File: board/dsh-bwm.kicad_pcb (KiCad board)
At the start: 2 copper layers, 121.3 x 78.7 mm, 36 parts, among them IC1 TPS5450DDA, IC2 MAX485CSA+T, J1 MPM-15-24, J2 Power, J3 Connections, J4 LED, J5 SWD6p, K1 833H-1C-C-24VDC, K2 833H-1C-C-24VDC, K3 833H-1C-C-24VDC, K4 833H-1C-C-24VDC, Q1 IRLB8721PBF, SW1 BOOTSEL, U1 RP2040_Stamp

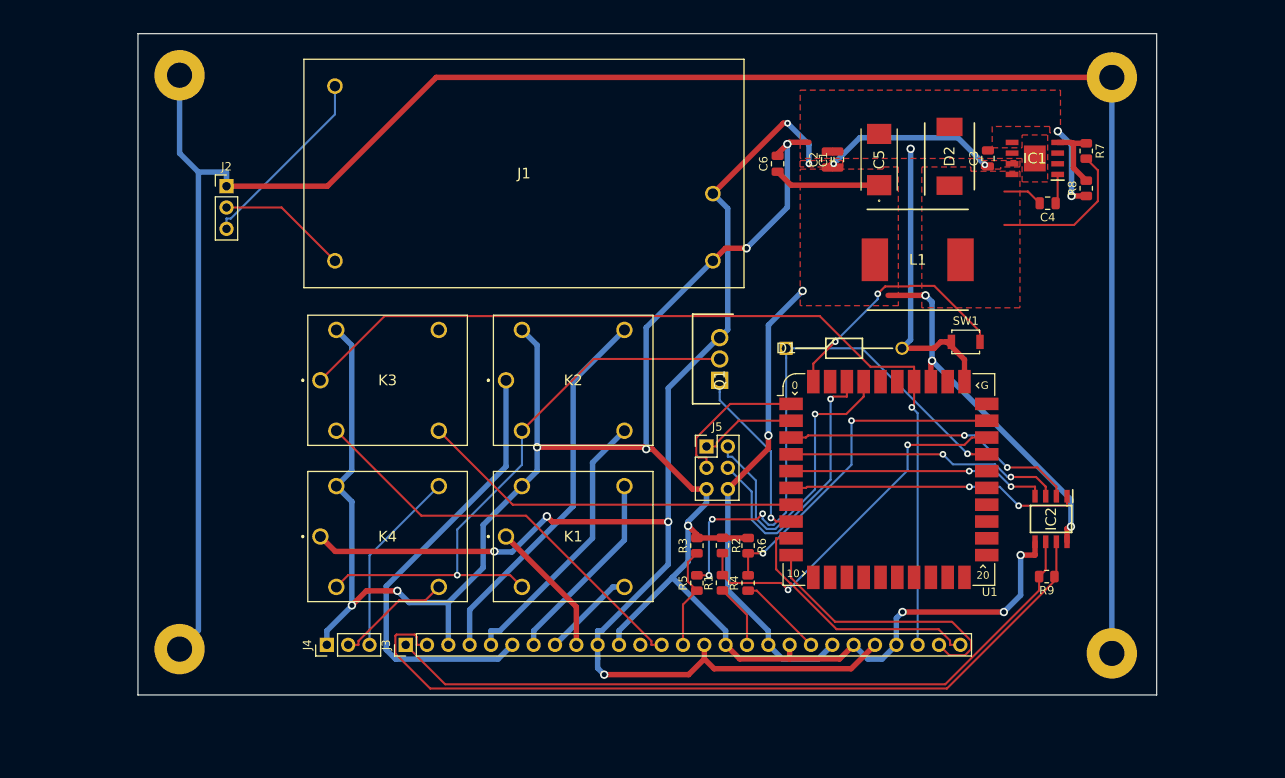
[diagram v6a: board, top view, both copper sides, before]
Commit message: board update, modbus address selector
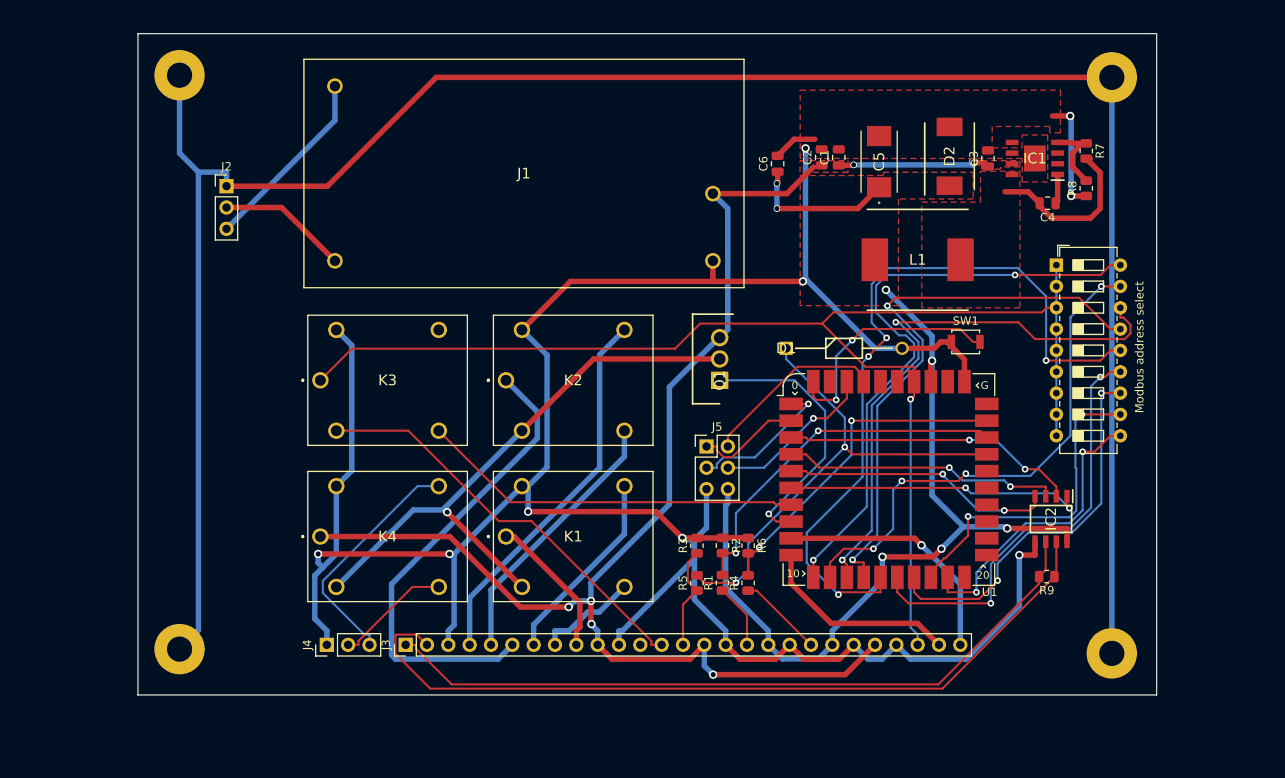
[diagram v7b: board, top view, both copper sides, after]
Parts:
- added Modbus address select: SW_DIP_x09, Button_Switch_THT:SW_DIP_SPSTx09_Slide_6.7x24.42mm_W7.62mm_P2.54mm_LowProfile, F.Cu at (200.9, 82.8)
- moved C2 0.77 mm to (173.0, 70.0)
- moved C1 0.30 mm to (175.0, 70.0)
- moved C5 0.25 mm to (179.8, 70.5)
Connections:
- D2 pad 1: /Power/5Vunf -> 5V
- U1 pad 11: unconnected-(U1-Pad11) -> MBADRB1
- U1 pad 12: unconnected-(U1-Pad12) -> MBADRB2
- U1 pad 13: unconnected-(U1-Pad13) -> MBADRB3
- U1 pad 14: unconnected-(U1-Pad14) -> MBADRB4
- U1 pad 15: unconnected-(U1-Pad15) -> MBADRB5
- U1 pad 16: unconnected-(U1-Pad16) -> MBADRB7
- U1 pad 17: unconnected-(U1-Pad17) -> MBADRB6
- U1 pad 18: unconnected-(U1-Pad18) -> MBADRB8
- U1 pad 19: unconnected-(U1-Pad19) -> MBADRB9
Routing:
- net MBADRB5: track 0.00 -> 90.0 mm, vias 0 -> 4
- net MBADRB1: track 0.00 -> 72.2 mm, vias 0 -> 2
- net MBADRB3: track 0.00 -> 68.5 mm, vias 0 -> 2
- net MBADRB4: track 0.00 -> 68.4 mm, vias 0 -> 2
- net MBADRB2: track 0.00 -> 61.2 mm, vias 0 -> 4
- net MBADRB7: track 0.00 -> 51.5 mm, vias 0 -> 2
- net 3v3: track 109.9 -> 158.3 mm
- net MBADRB6: track 0.00 -> 45.7 mm, vias 0 -> 2
- net MBADRB8: track 0.00 -> 38.8 mm, vias 0 -> 2
- net MBADRB9: track 0.00 -> 35.5 mm, vias 0 -> 2
- net 24V: track 186.0 -> 167.8 mm, vias 8 -> 6
- net SWDIO: track 37.1 -> 22.0 mm, vias 1 -> 0
- net GND: track 307.5 -> 321.5 mm, vias 13 -> 9
- net SWCLK: track 33.5 -> 19.6 mm
- net ALARM: track 21.5 -> 32.2 mm
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
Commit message: TPs, vias, some comments on board, fml
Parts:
- removed the J3 at (123.4, 128.0)
- removed Modbus address select: SW_DIP_x09, Button_Switch_THT:SW_DIP_SPSTx09_Slide_6.7x24.42mm_W7.62mm_P2.54mm_LowProfile
- removed the R1 at (161.2, 120.6)
- removed the R2 at (161.2, 116.2)
- added IC2: AT24C256C-SSHL-T, SamacSys_Parts:SOIC127P600X175-8N, F.Cu at (207.8, 115.6)
- added J1: USB_A, Connector_USB:USB_A_Molex_105057_Vertical, F.Cu at (164.0, 82.0)
- added J6: Connections, Connector_PinHeader_2.54mm:PinHeader_1x39_P2.54mm_Vertical, F.Cu at (99.0, 131.8)
- added K1: T81N5D312, SamacSys_Parts:T81H5D31212, F.Cu at (104.8, 123.8)
- added K6: T81N5D312, SamacSys_Parts:T81H5D31212, F.Cu at (122.4, 123.8)
- added K7: T81N5D312, SamacSys_Parts:T81H5D31212, F.Cu at (140.2, 110.6)
- added K8: T81N5D312, SamacSys_Parts:T81H5D31212, F.Cu at (140.2, 97.4)
- added Q1: IRLB8721PBF, SamacSys_Parts:TO254P483X1016X1994-3P, F.Cu at (140.8, 123.3)
- added Q2: IRLB8721PBF, SamacSys_Parts:TO254P483X1016X1994-3P, F.Cu at (140.8, 117.3)
- added Q4: IRLB8721PBF, SamacSys_Parts:TO254P483X1016X1994-3P, F.Cu at (152.8, 122.0)
- added Q5: IRLB8721PBF, SamacSys_Parts:TO254P483X1016X1994-3P, F.Cu at (158.6, 102.2)
- added Q6: IRLB8721PBF, SamacSys_Parts:TO254P483X1016X1994-3P, F.Cu at (158.6, 108.4)
- added R5: 10k, Resistor_SMD:R_0805_2012Metric, F.Cu at (206.6, 122.0)
- added R7: 2k, Resistor_SMD:R_0805_2012Metric, F.Cu at (158.0, 119.1)
- added R8: 1k, Resistor_SMD:R_0805_2012Metric, F.Cu at (162.6, 119.1)
- added R9: 2k, Resistor_SMD:R_0805_2012Metric, F.Cu at (162.6, 123.0)
- added SW2: RESET, Button_Switch_SMD:SW_SPST_B3U-1000P, F.Cu at (191.8, 95.3)
- added TP1: RO, TestPoint:TestPoint_Pad_D1.5mm, F.Cu at (203.5, 108.4)
- added TP10: COND, TestPoint:TestPoint_Pad_D1.5mm, F.Cu at (166.0, 118.8)
- added TP11: ESCL, TestPoint:TestPoint_Pad_D1.5mm, F.Cu at (212.5, 113.3)
- added TP12: ESDA, TestPoint:TestPoint_Pad_D1.5mm, F.Cu at (212.3, 118.0)
- added TP13: PSin, TestPoint:TestPoint_Pad_D1.5mm, F.Cu at (166.2, 89.5)
- added TP14: D-, TestPoint:TestPoint_Pad_D1.5mm, F.Cu at (176.8, 91.6)
- added TP15: D+, TestPoint:TestPoint_Pad_D1.5mm, F.Cu at (172.8, 91.5)
- added TP16: PSout, TestPoint:TestPoint_Pad_D1.5mm, F.Cu at (166.4, 94.6)
- added TP17: 5V, TestPoint:TestPoint_Pad_D1.5mm, F.Cu at (172.6, 83.5)
- added TP2: RE, TestPoint:TestPoint_Pad_D1.5mm, F.Cu at (209.7, 108.2)
- added TP3: DE, TestPoint:TestPoint_Pad_D1.5mm, F.Cu at (206.6, 108.3)
- added TP4: DI, TestPoint:TestPoint_Pad_D1.5mm, F.Cu at (200.3, 108.5)
- added TP5: 4-20mA, TestPoint:TestPoint_Pad_D1.5mm, F.Cu at (165.9, 124.2)
- added TP6: GND, TestPoint:TestPoint_Pad_D1.5mm, F.Cu at (173.0, 65.1)
- added TP7: 24V, TestPoint:TestPoint_Pad_D1.5mm, F.Cu at (163.0, 65.2)
- added TP8: B, TestPoint:TestPoint_Pad_D1.5mm, F.Cu at (202.8, 125.7)
- added TP9: A, TestPoint:TestPoint_Pad_D1.5mm, F.Cu at (199.1, 125.6)
- J3: renamed from J2; footprint Connector_PinHeader_2.54mm:PinHeader_1x03_P2.54mm_Vertical -> TBP03R2-350-03BE:CUI_TBP03R2-350-03BE
- J4: footprint Connector_PinHeader_2.54mm:PinHeader_1x03_P2.54mm_Vertical -> TBP03R2-350-03BE:CUI_TBP03R2-350-03BE
- K2: renamed from K3; value 833H-1C-C-24VDC -> T81N5D312; footprint SamacSys_Parts:833H1CC24VDC -> SamacSys_Parts:T81H5D31212
- K3: renamed from K1; value 833H-1C-C-24VDC -> T81N5D312; footprint SamacSys_Parts:833H1CC24VDC -> SamacSys_Parts:T81H5D31212
- K4: renamed from K2; value 833H-1C-C-24VDC -> T81N5D312; footprint SamacSys_Parts:833H1CC24VDC -> SamacSys_Parts:T81H5D31212
- K5: renamed from K4; value 833H-1C-C-24VDC -> T81N5D312; footprint SamacSys_Parts:833H1CC24VDC -> SamacSys_Parts:T81H5D31212
- R4: value 1k -> 10k
- R6: value 2k -> 1k
- SW1: value BOOTSEL -> ModBus address selector; footprint Button_Switch_SMD:SW_SPST_B3U-1000P -> Button_Switch_THT:SW_DIP_SPSTx07_Slide_6.7x19.34mm_W7.62mm_P2.54mm_LowProfile
- moved R4 45.4 mm to (209.5, 122.0), turned to -90 degrees
- moved J4 41.7 mm to (90.9, 93.3)
- moved Q3 18.0 mm to (158.6, 114.3), turned to 0 degrees
- moved J5 14.7 mm to (158.7, 89.7)
- moved H3 14.7 mm to (83.6, 135.5)
- moved K3 13.7 mm to (122.4, 110.6)
- moved K4 13.0 mm to (122.4, 97.4)
- moved H1 12.8 mm to (83.7, 60.2)
- moved J3 12.4 mm to (90.9, 78.8), turned to 90 degrees
- moved SW1 11.0 mm to (199.6, 86.4)
- moved K5 9.63 mm to (104.8, 110.6)
- moved R6 9.26 mm to (158.0, 123.1), turned to 90 degrees
- moved K2 8.56 mm to (104.8, 97.4)
- moved J2 7.99 mm to (152.0, 74.3)
- moved H2 5.91 mm to (207.4, 134.9)
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- renumbered IC2 to IC1, IC1 to IC3, J1 to J2, Q1 to Q3, R3 to R1, R7 to R10, R8 to R11, R5 to R2, R9 to R3
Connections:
- K2 pad 1: 3v3 -> unconnected-(K2-Pad1)
- K2 pad 2: ZDSENSE -> ZD
- K2 pad 3: ZD -> 3v3
- K2 pad 4: unconnected-(K3-Pad4) -> ZDSENSE
- K3 pad 1: AlarmC1 -> LekNC
- K3 pad 2: Net-(K1-Pad2) -> LekNO
- K3 pad 3: AlarmNO1 -> LekC
- K3 pad 4: AlarmNC1 -> Net-(K3-Pad4)
- K4 pad 1: AlarmC2 -> AlarmNC
- K4 pad 2: Net-(K1-Pad2) -> AlarmNO
- K4 pad 3: AlarmNO2 -> AlarmC
- K4 pad 4: AlarmNC2 -> Net-(K4-Pad4)
- K5 pad 1: 24V -> R
- K5 pad 2: Net-(K1-Pad2) -> G
- K5 pad 3: G -> 24V
- K5 pad 4: R -> Net-(K4-Pad4)
- Q3 pad 2: Net-(K1-Pad2) -> Net-(K4-Pad4)
- R10 pad 2: /Power/5Vunf -> 5V
- R4 pad 1: PressureOUT -> 5V
- R4 pad 2: PSout -> EEPROMSDA
- R6 pad 1: GND -> PressureIN
- R6 pad 2: PSout -> PSin
- SW1 pad 1: GND -> 3v3
- SW1 pad 2: Net-(SW1-Pad2) -> 3v3
- U1 pad 10: LDNC -> unconnected-(U1-Pad10)
- U1 pad 11: MBADRB1 -> EEPROMSDA
- U1 pad 12: MBADRB2 -> EEPROMSCL
- U1 pad 13: MBADRB3 -> MBADRB1
- U1 pad 14: MBADRB4 -> MBADRB2
- U1 pad 15: MBADRB5 -> MBADRB3
- U1 pad 16: MBADRB7 -> MBADRB4
- U1 pad 17: MBADRB6 -> MBADRB5
- U1 pad 18: MBADRB8 -> MBADRB6
- U1 pad 19: MBADRB9 -> MBADRB7
- U1 pad 20: unconnected-(U1-Pad20) -> ALARM
- U1 pad 21: unconnected-(U1-Pad21) -> ALARMLEK
- U1 pad 22: unconnected-(U1-Pad22) -> ALARMZOUT
- U1 pad 23: unconnected-(U1-Pad23) -> ALARMDRUKIN
- U1 pad 24: unconnected-(U1-Pad24) -> ALARMDRUKUIT
- U1 pad 25: unconnected-(U1-Pad25) -> ALARMCOND
- U1 pad 35: unconnected-(U1-Pad35) -> Net-(U1-Pad35)
- U1 pad 36: unconnected-(U1-Pad36) -> Net-(U1-Pad36)
- U1 pad 39: RESET -> Net-(U1-Pad39)
- U1 pad 40: Net-(SW1-Pad2) -> unconnected-(U1-Pad40)
- U1 pad 8: ALARM -> LDNO
- U1 pad 9: LDNO -> LDNC
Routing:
- net 5V: track 120.1 -> 236.9 mm, vias 7 -> 11
- net DrukUitNC: track 0.00 -> 98.8 mm
- net ZoutNO: track 0.00 -> 95.8 mm
- net GND: track 321.5 -> 409.6 mm, vias 9 -> 13
- net DrukUitNO: track 0.00 -> 87.2 mm
- net Net-(K4-Pad4): track 0.00 -> 81.5 mm
- net PressureOUT: track 10.2 -> 90.7 mm, vias 0 -> 3
- net AlarmC: track 0.00 -> 77.7 mm
- net DrukUitC: track 0.00 -> 75.9 mm, vias 0 -> 1
- net ZoutC: track 0.00 -> 70.5 mm
- net ZoutNC: track 0.00 -> 70.1 mm
- net Net-(K1-Pad2): track 70.0 -> 0.00 mm, vias 1 -> 0
- net 4-20mA input: track 13.7 -> 81.9 mm, vias 0 -> 2
- net ALARMLEK: track 0.00 -> 65.6 mm, vias 0 -> 2
- net PSin: track 43.2 -> 107.2 mm, vias 2 -> 6
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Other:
- board size 121.3 x 78.7 mm -> 137.4 x 88.5 mm
- board text added: "1"
- board text added: "2"
- board text added: "3"
- board text added: "4"
- board text added: "5"
- board text added: "6"
- board text added: "7"
- board text added: "A"
- board text added: "Alarm"
- board text added: "Alarm Conduct."
- board text added: "Alarm DrukIN"
- board text added: "Alarm DrukUIT"
- board text added: "Alarm Waterlek"
- board text added: "Alarm Zoutdet."
- board text added: "B"
- board text added: "C"
- board text added: "Conduct."
- board text added: "DSH Belgium Leandro Marceddu DSH WaterManager (v0.1)"
- board text added: "DrukIN"
- board text added: "DrukUIT"
- board text added: "GND"
- board text added: "ModBus"
- board text added: "NC"
- board text added: "NO"
- board text added: "WaterDet."
- board text added: "ZoutDet."
